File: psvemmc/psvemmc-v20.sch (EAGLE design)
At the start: 43 parts, among them J1 CON_HEADER_2X10-SHROUDED, U1 USB2244QFN, U2 LP3996_DSC_10, U3 TXS02612, X1 ZX62D-B-5PA8, Y1 XRCGB

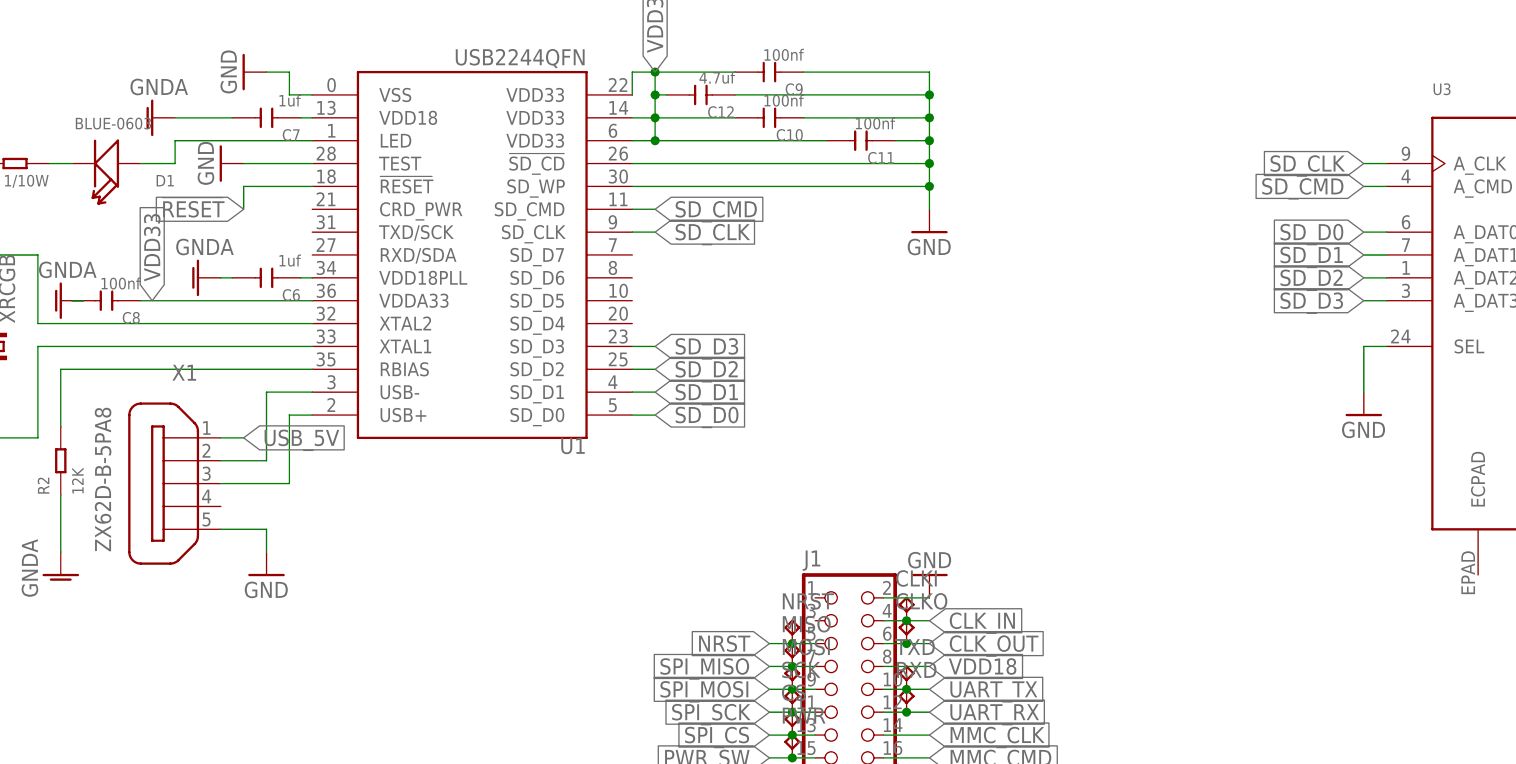
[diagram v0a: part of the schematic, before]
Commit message: psvemmc v2.1: added EEPROM and GND pad
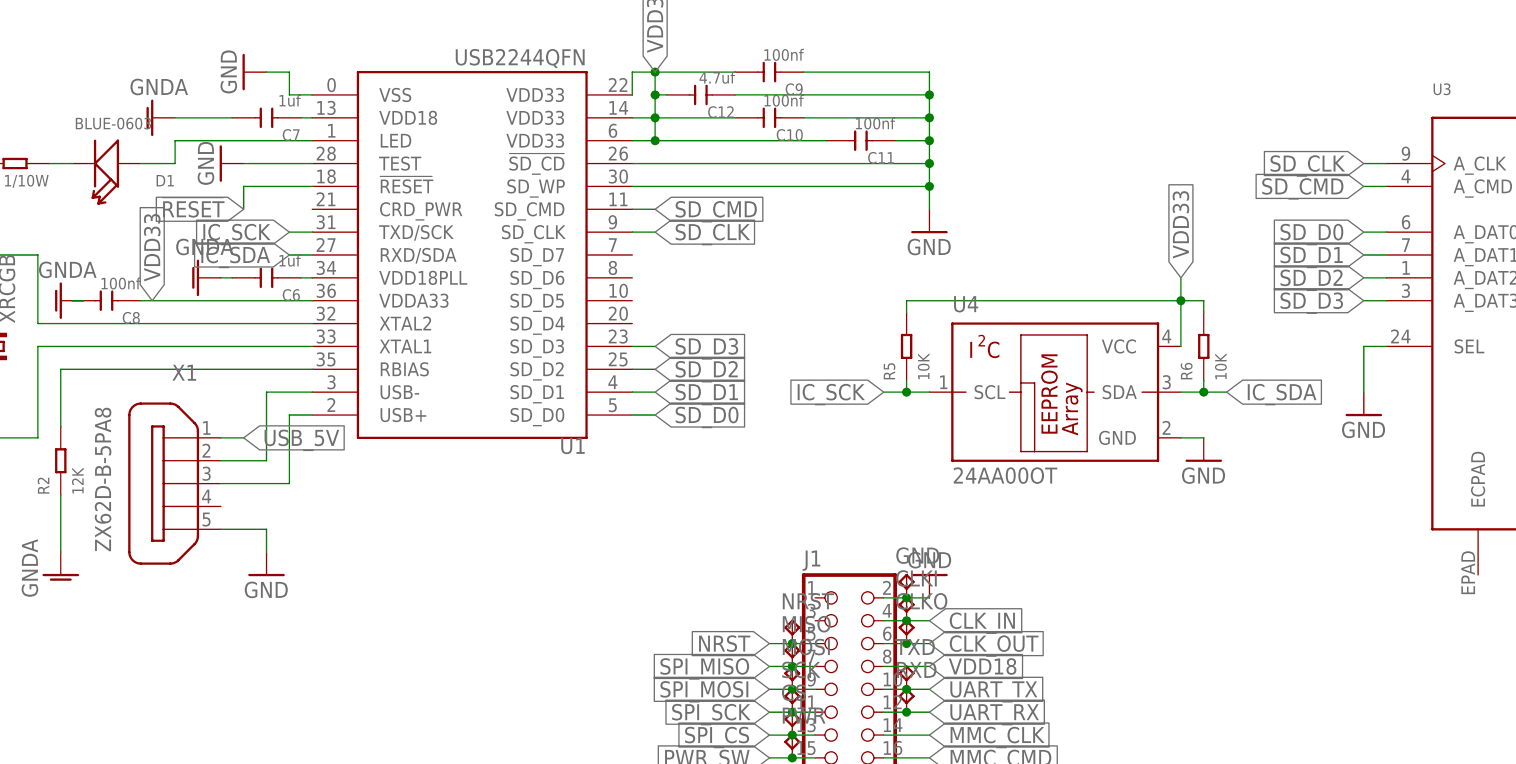
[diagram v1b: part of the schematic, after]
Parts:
- added GND: TPTP10R, testpad:TPTP10R
- added R5, R6: 10K, Seeed-Resistor:SMD-RES-10K-1%-1/10W(0603)
- added U4: 24AA00OT, microchip:24AA00OT
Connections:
- new net IC_SCK: R5.1, U1.TXD/SCK, U4.SCL
- new net IC_SDA: R6.1, U1.RXD/SDA, U4.SDA
- net GND: now also GND.TP, U4.GND
- net VDD33: now also R5.2, R6.2, U4.VCC
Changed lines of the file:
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@@
 </class>
 <class number="1" name="USB" width="0" drill="0">
-<clearance class="0" value="0.508"/>
 </class>
 <class number="2" name="GND" width="0" drill="0">
-<clearance class="1" value="0.508"/>
 </class>
 </classes>
@@
 <part name="JP1" library="jumper" library_urn="urn:adsk.eagle:library:252" deviceset="JP1Q" device="" package3d_urn="urn:adsk.eagle:package:15455/1"/>
 <part name="GND23" library="supply1" library_urn="urn:adsk.eagle:library:371" deviceset="GND" device=""/>
+<part name="GND" library="testpad" library_urn="urn:adsk.eagle:library:385" deviceset="TP" device="TP10R" package3d_urn="urn:adsk.eagle:package:27959/1"/>
+<part name="U4" library="microchip" library_urn="urn:adsk.eagle:library:294" deviceset="24*00" device="OT" package3d_urn="urn:adsk.eagle:package:20809/2" technology="AA"/>
+<part name="R5" library="Seeed-Resistor" deviceset="SMD-RES-10K-1%-1/10W(0603)" device="" value="10K"/>
+<part name="R6" library="Seeed-Resistor" deviceset="SMD-RES-10K-1%-1/10W(0603)" device="" value="10K"/>
+<part name="GND24" library="supply1" library_urn="urn:adsk.eagle:library:371" deviceset="GND" device=""/>
 </parts>
 <sheets>
@@
 <instance part="JP1" gate="A" x="165.1" y="137.16" rot="R90"/>
 <instance part="GND23" gate="1" x="175.26" y="134.62"/>
+<instance part="GND" gate="G$1" x="127" y="45.72"/>
+<instance part="U4" gate="G$1" x="142.24" y="66.04"/>
+<instance part="R5" gate="G$1" x="127" y="71.12" rot="R90"/>
+<instance part="R6" gate="G$1" x="160.02" y="71.12" rot="R90"/>
+<instance part="GND24" gate="1" x="160.02" y="58.42"/>
 </instances>
 <busses>
@@
 <segment>
 <pinref part="J1" gate="J" pin="2"/>
-<wire x1="124.46" y1="43.18" x2="129.54" y2="43.18" width="0.1524" layer="91"/>
+<wire x1="124.46" y1="43.18" x2="127" y2="43.18" width="0.1524" layer="91"/>
 <pinref part="GND19" gate="1" pin="GND"/>
+<pinref part="GND" gate="G$1" pin="TP"/>
+<wire x1="127" y1="43.18" x2="129.54" y2="43.18" width="0.1524" layer="91"/>
+<junction x="127" y="43.18"/>
 </segment>
 <segment>
@@
 <wire x1="15.24" y1="71.12" x2="15.24" y2="72.39" width="0.1524" layer="91"/>
 <junction x="15.24" y="71.12"/>
+</segment>
+<segment>
+<pinref part="U4" gate="G$1" pin="GND"/>
+<pinref part="GND24" gate="1" pin="GND"/>
+<wire x1="157.48" y1="60.96" x2="160.02" y2="60.96" width="0.1524" layer="91"/>
 </segment>
 </net>
@@
 <label x="198.12" y="104.14" size="1.778" layer="95" rot="R90" xref="yes"/>
 </segment>
+<segment>
+<pinref part="U4" gate="G$1" pin="VCC"/>
+<wire x1="157.48" y1="71.12" x2="157.48" y2="76.2" width="0.1524" layer="91"/>
+<pinref part="R6" gate="G$1" pin="2"/>
+<wire x1="157.48" y1="76.2" x2="160.02" y2="76.2" width="0.1524" layer="91"/>
+<wire x1="160.02" y1="76.2" x2="160.02" y2="74.93" width="0.1524" layer="91"/>
+<wire x1="157.48" y1="76.2" x2="127" y2="76.2" width="0.1524" layer="91"/>
+<junction x="157.48" y="76.2"/>
+<pinref part="R5" gate="G$1" pin="2"/>
+<wire x1="127" y1="76.2" x2="127" y2="74.93" width="0.1524" layer="91"/>
+<wire x1="157.48" y1="76.2" x2="157.48" y2="78.74" width="0.1524" layer="91"/>
+<label x="157.48" y="78.74" size="1.778" layer="95" rot="R90" xref="yes"/>
+</segment>
 </net>
 <net name="!RESET" class="0">
@@
 </segment>
 </net>
+<net name="IC_SCK" class="0">
+<segment>
+<pinref part="U1" gate="G$1" pin="TXD/SCK"/>
+<wire x1="60.96" y1="83.82" x2="58.42" y2="83.82" width="0.1524" layer="91"/>
+<label x="58.42" y="83.82" size="1.778" layer="95" rot="R180" xref="yes"/>
+</segment>
+<segment>
+<pinref part="U4" gate="G$1" pin="SCL"/>
+<wire x1="129.54" y1="66.04" x2="127" y2="66.04" width="0.1524" layer="91"/>
+<wire x1="127" y1="66.04" x2="127" y2="67.31" width="0.1524" layer="91"/>
+<pinref part="R5" gate="G$1" pin="1"/>
+<wire x1="127" y1="66.04" x2="124.46" y2="66.04" width="0.1524" layer="91"/>
+<junction x="127" y="66.04"/>
+<label x="124.46" y="66.04" size="1.778" layer="95" rot="R180" xref="yes"/>
+</segment>
+</net>
+<net name="IC_SDA" class="0">
+<segment>
+<pinref part="U1" gate="G$1" pin="RXD/SDA"/>
+<wire x1="60.96" y1="81.28" x2="58.42" y2="81.28" width="0.1524" layer="91"/>
+<label x="58.42" y="81.28" size="1.778" layer="95" rot="R180" xref="yes"/>
+</segment>
+<segment>
+<pinref part="U4" gate="G$1" pin="SDA"/>
+<wire x1="157.48" y1="66.04" x2="160.02" y2="66.04" width="0.1524" layer="91"/>
+<wire x1="160.02" y1="66.04" x2="162.56" y2="66.04" width="0.1524" layer="91"/>
+<wire x1="160.02" y1="66.04" x2="160.02" y2="67.31" width="0.1524" layer="91"/>
+<junction x="160.02" y="66.04"/>
+<pinref part="R6" gate="G$1" pin="1"/>
+<label x="162.56" y="66.04" size="1.778" layer="95" xref="yes"/>
+</segment>
+</net>
